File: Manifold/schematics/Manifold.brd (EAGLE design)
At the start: 56 x 100 mm, 124 parts, among them IC1 MC7805CDTG, IC2 NE5532D, IC3 NE5532D, IC4 QUAD_OPAMPD, IC5 LM4040B10, IC6 TL072D, Q1 BSS123, Q2 SI2309CDS

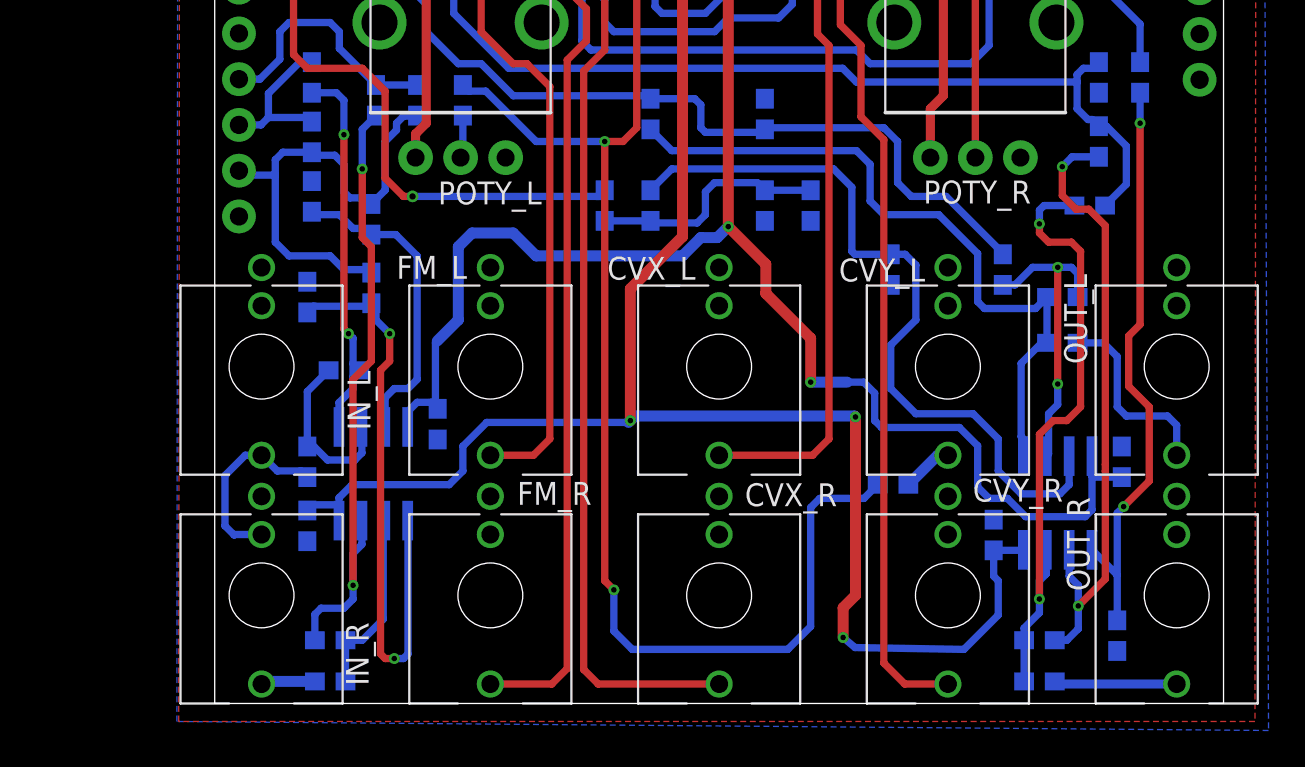
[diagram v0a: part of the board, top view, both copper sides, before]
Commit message: change resistor value
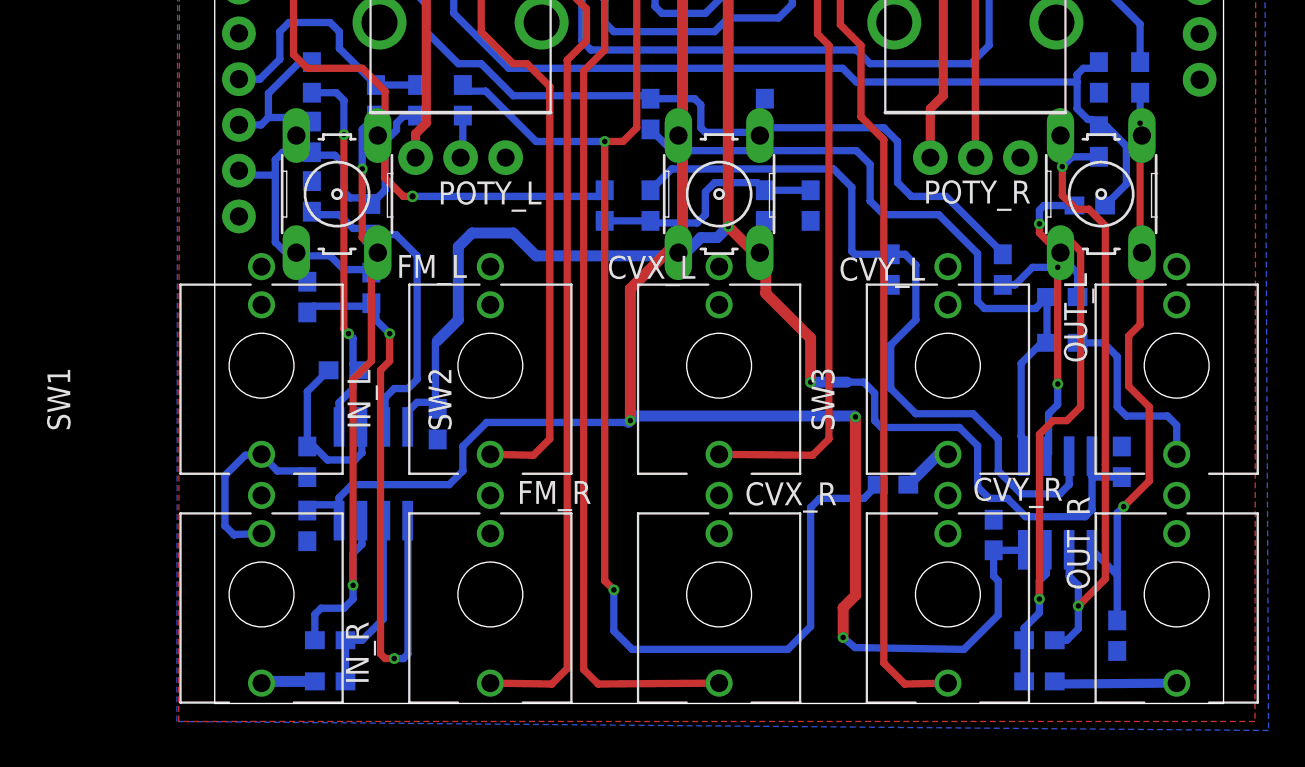
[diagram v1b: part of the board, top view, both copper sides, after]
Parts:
- added SW1, SW2, SW3: (no value), switch-omron:B3F-10XX
- R16, R19, R22, R26: value 4k3 -> 4k7
- moved CVX_L 0.05 mm to (27.9, 17.8)
- moved CVY_L 0.05 mm to (40.6, 17.8)
- moved FM_L 0.05 mm to (15.2, 17.8)
- moved IN_L 0.05 mm to (2.54, 17.8)
- moved OUT_L 0.05 mm to (53.3, 17.8)
- moved CVX_R 0.05 mm to (27.9, 5.08)
- moved CVY_R 0.05 mm to (40.6, 5.08)
- moved FM_R 0.05 mm to (15.2, 5.08)
- moved IN_R 0.05 mm to (2.54, 5.08)
- moved OUT_R 0.05 mm to (53.3, 5.08)
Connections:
- new net A7_SW2: SW1.1, SW1.2, SW2.1, SW2.2, SW3.1, SW3.2
- net GND: now also SW1.3, SW1.4, SW2.3, SW2.4, SW3.3, SW3.4
